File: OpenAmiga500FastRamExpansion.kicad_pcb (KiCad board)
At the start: 2 copper layers, 99.7 x 69.1 mm, 35 parts, among them J1 68000_SOCKET, P1 JTAG_CONNECTOR, P99 OSHW_LOGO, U1 68000D, U2 74LS157, U3 74LS157, U4 ATF1502AS-10JU44, U5 HYB5118160BSJ, U6 HYB5118160BSJ, U7 HYB5118160BSJ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

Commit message: Completed routing of data bus from CPU to RAM
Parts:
- moved C2 135.5 mm to (146.2, 68.8)
- moved C3 68.7 mm to (176.7, 68.8)
- moved C15 9.20 mm to (238.6, 58.8)
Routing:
- net /d11: track 53.2 -> 92.7 mm, vias 0 -> 1
- net /d12: track 53.1 -> 90.0 mm, vias 0 -> 1
- net /d13: track 53.2 -> 89.3 mm, vias 0 -> 1
- net /d14: track 53.2 -> 88.4 mm, vias 0 -> 1
- net /d15: track 53.1 -> 86.5 mm, vias 0 -> 1
- net VCC: track 7.11 -> 14.6 mm
- net /d10: track 96.0 -> 94.2 mm
- net /d8: track 98.5 -> 96.9 mm
- net /d9: track 97.3 -> 96.5 mm

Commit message: Almost there...
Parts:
- C13, C14, C15, C16, C17, C18, C19, C5, C6, C8: moved to B.Cu
- U4: footprint Package_LCC:PLCC-44_THT-Socket -> OpenAmiga500FastRamExpansion:PLCC-44_THT-Socket
- moved C19 185.7 mm to (111.2, 113.3), turned to 0 degrees
- moved C12 149.2 mm to (142.7, 94.2), turned to 0 degrees
- moved C8 141.0 mm to (159.3, 94.2), turned to 0 degrees
- moved C11 138.1 mm to (142.7, 87.9)
- moved C9 121.0 mm to (159.3, 87.9)
- moved C15 116.8 mm to (127.2, 93.7)
- moved C10 115.0 mm to (159.3, 113.3), turned to 0 degrees
- moved C18 110.3 mm to (111.2, 94.2)
- moved C5 107.0 mm to (180.7, 101.6), turned to 180 degrees
- moved C17 105.2 mm to (111.2, 87.9)
- moved C16 103.2 mm to (127.2, 113.3)
- moved C7 97.3 mm to (170.3, 98.8), turned to 90 degrees
- moved C13 94.7 mm to (142.7, 113.3), turned to 0 degrees
- moved C1 94.3 mm to (103.1, 117.2)
- moved C14 90.1 mm to (127.2, 87.9)
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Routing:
- net VCC: track 14.6 -> 523.3 mm, vias 0 -> 14
- net /a23: track 3.56 -> 117.0 mm
- net /a22: track 3.56 -> 110.4 mm
- net /a21: track 3.56 -> 104.4 mm
- net /~as: track 3.56 -> 98.9 mm
- net /a17: track 3.56 -> 91.3 mm, vias 0 -> 1
- net /a20: track 3.56 -> 91.1 mm
- net /~uds: track 3.56 -> 90.3 mm
- net /~ras3: track 0.00 -> 86.0 mm, vias 0 -> 1
- net /a19: track 3.56 -> 84.9 mm
- net /a18: track 17.2 -> 97.8 mm
- net /~ras2: track 0.00 -> 74.1 mm, vias 0 -> 1
- net /a16: track 11.8 -> 84.5 mm
- net /~ras1: track 0.00 -> 69.7 mm, vias 0 -> 1
- net /~lds: track 3.56 -> 71.0 mm
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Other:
- board size 99.7 x 69.1 mm -> 99.7 x 71.2 mm

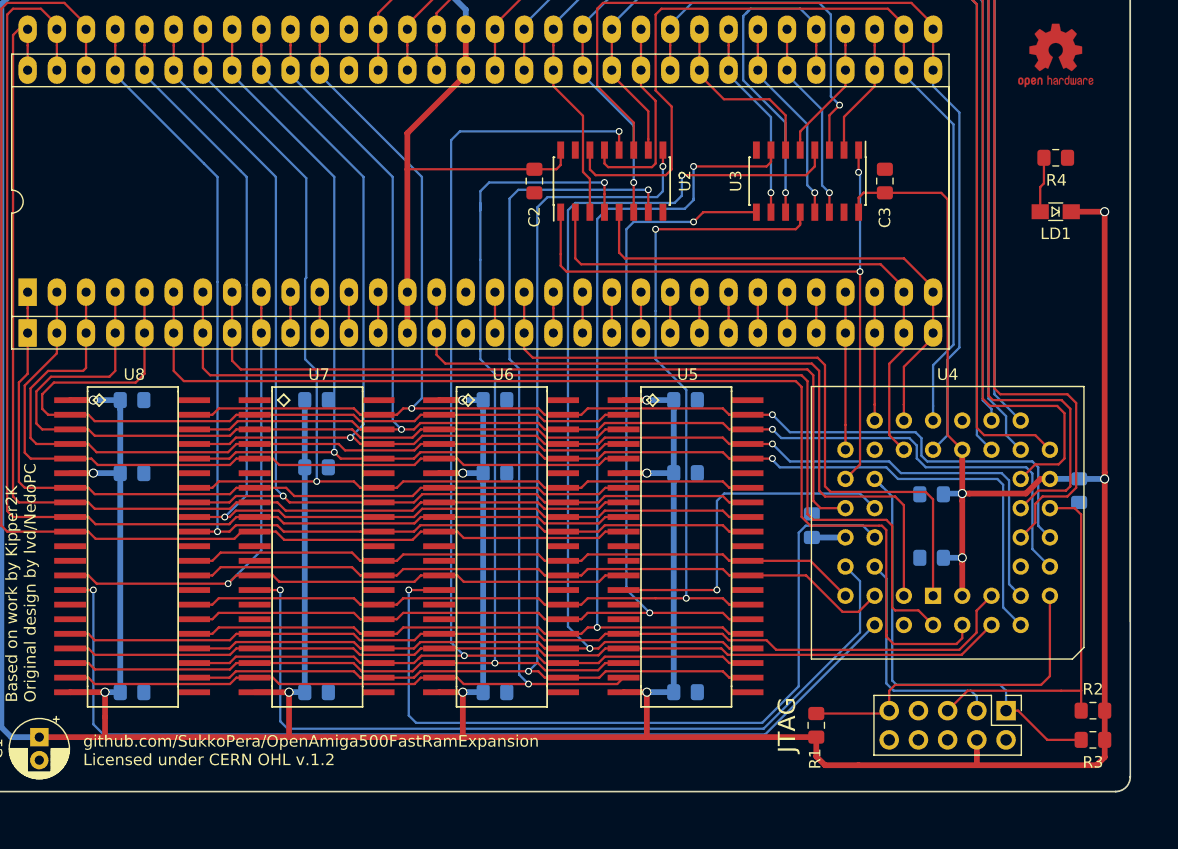
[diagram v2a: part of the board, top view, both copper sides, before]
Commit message: Routing complete Ground stitching and some refinements TBD
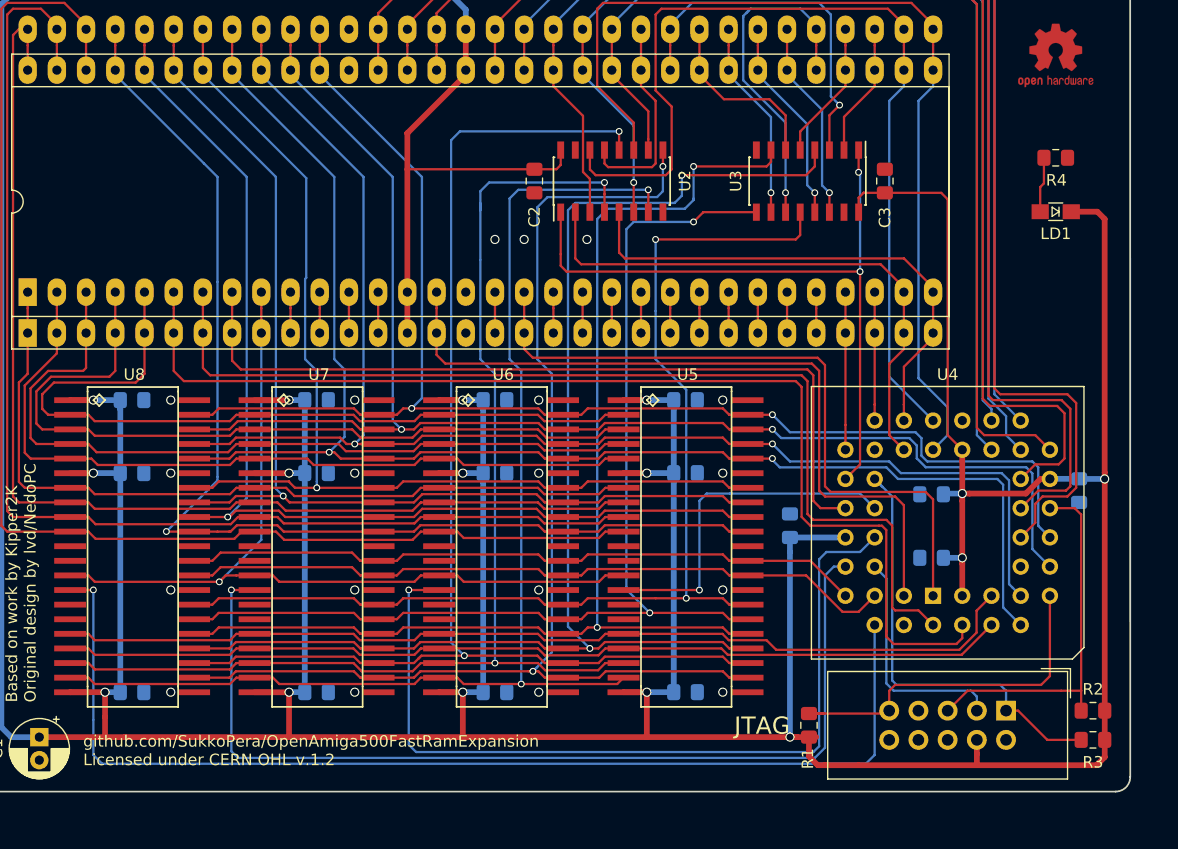
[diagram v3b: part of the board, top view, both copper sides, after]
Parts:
- P1: footprint Connector_PinHeader_2.54mm:PinHeader_2x05_P2.54mm_Vertical -> Connector_IDC:IDC-Header_2x05_P2.54mm_Vertical
- moved C8 6.35 mm to (159.3, 87.9)
- moved C9 6.35 mm to (159.3, 94.2)
- moved C7 1.91 mm to (168.4, 98.8)
- moved R1 0.63 mm to (170.1, 116.2)
- moved C15 0.51 mm to (127.2, 94.2)
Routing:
- net VCC: track 523.3 -> 551.6 mm, vias 14 -> 16
- net /~ras2: track 74.1 -> 85.4 mm
- net /~ras3: track 86.0 -> 96.3 mm
- net /~ras1: track 69.7 -> 74.1 mm
- net /d8: track 96.9 -> 101.1 mm
- net /d13: track 123.8 -> 125.8 mm
- net /ma4: track 105.3 -> 106.7 mm
- net /jtag_tdi: track 29.7 -> 30.9 mm
- net /d12: track 126.1 -> 127.0 mm
- net /d11: track 93.0 -> 93.6 mm
- net GND: vias 0 -> 19

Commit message: Refinements here and there
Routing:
- net /ma4: track 106.7 -> 106.1 mm

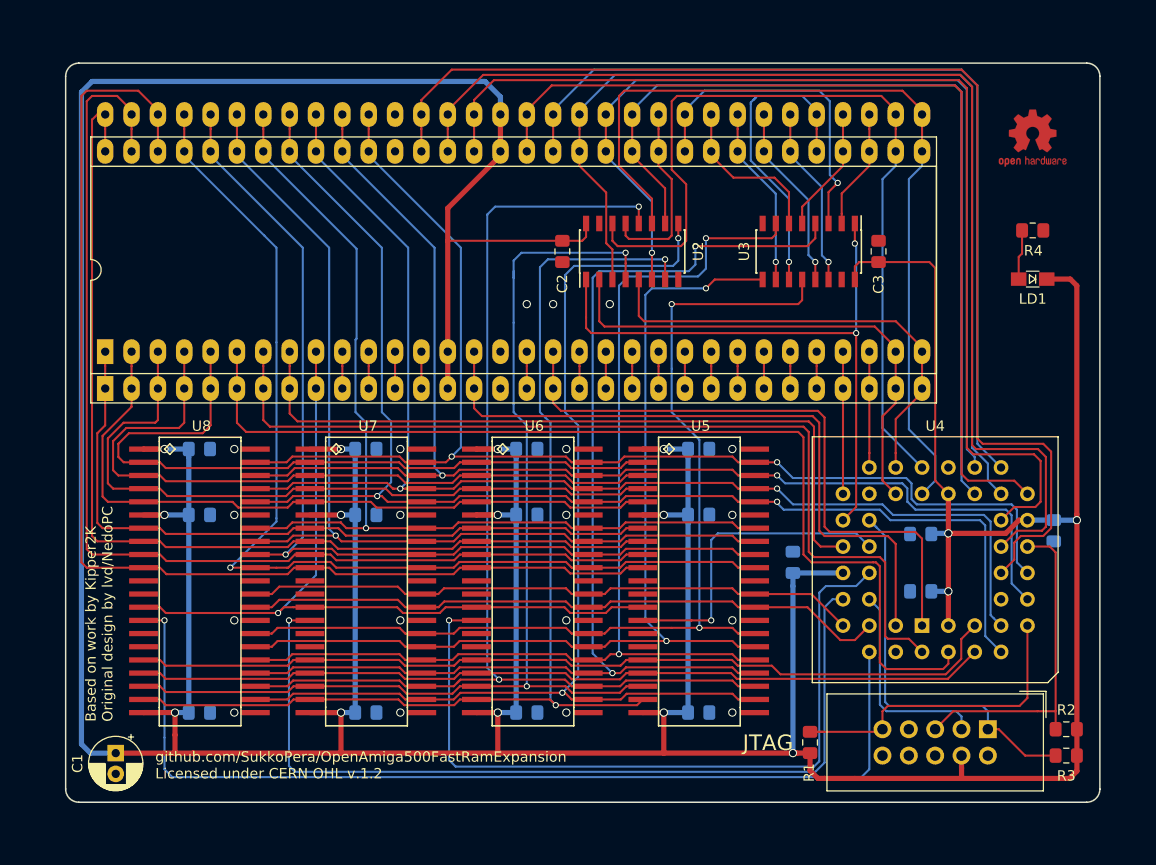
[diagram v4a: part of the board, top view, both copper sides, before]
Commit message: Stitched perimeter and more refinements
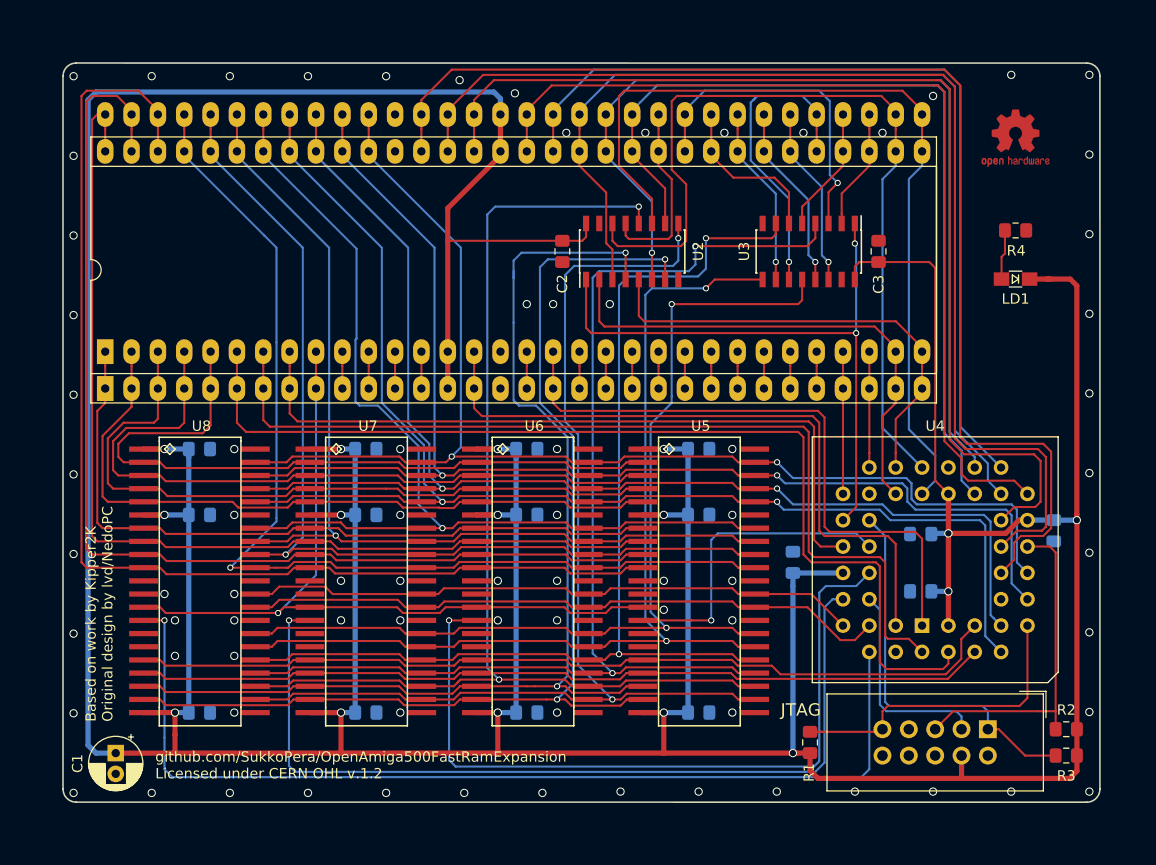
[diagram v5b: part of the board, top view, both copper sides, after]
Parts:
- moved LD1 1.65 mm to (189.9, 71.5)
- moved P99 1.65 mm to (189.9, 57.9)
- moved R4 1.65 mm to (189.9, 66.8)
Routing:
- net /d11: track 93.6 -> 97.7 mm
- net /ma2: track 105.6 -> 108.6 mm
- net /d12: track 127.0 -> 129.0 mm
- net /ma4: track 106.1 -> 107.5 mm
- net /d13: track 125.8 -> 126.9 mm
- net /a19: track 84.9 -> 83.9 mm
- net /a17: track 91.3 -> 90.3 mm
- net /a20: track 91.1 -> 90.1 mm
- net /a18: track 97.8 -> 96.8 mm
- net /a16: track 84.5 -> 83.5 mm
- net /ma3: track 106.7 -> 107.5 mm
- net VCC: track 551.3 -> 550.7 mm
- net /a21: track 104.4 -> 103.8 mm
- net GND: vias 19 -> 78
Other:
- board size 99.7 x 71.2 mm -> 100 x 71.3 mm

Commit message: More and more and more and more and more refinements...
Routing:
- net /d5: track 100.0 -> 96.0 mm
- net /~ras2: track 85.4 -> 84.8 mm
- net GND: vias 78 -> 84
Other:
- board size 100 x 71.3 mm -> 100 x 71.5 mm

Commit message: Add JTAG connector pinout
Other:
- board text added: "TCK"
- board text added: "TDI"
- board text added: "TDO"
- board text added: "TMS"
- board text removed: "1"
- board text removed: "1. TCK 2. GND 3. TDO 4. VCC"
- board text removed: "10"
- board text removed: "2"
- board text removed: "3"
- board text removed: "4"
- board text removed: "5"
- board text removed: "5. TMS 9. TDI 10. GND"
- board text removed: "6"
- board text removed: "7"
- board text removed: "8"
- board text removed: "9"
- board text removed: "JTAG PINOUT"
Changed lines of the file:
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@@
   (general
     (thickness 1.6)
-    (drawings 108)
+    (drawings 90)
     (tracks 1421)
     (zones 0)
@@
     )
   )
+  (gr_text GND (at 177.038 119.38) (layer B.SilkS)
+    (effects (font (size 0.7 0.7) (thickness 0.15)) (justify mirror))
+  )
+  (gr_text GND (at 187.198 119.38) (layer B.SilkS)
+    (effects (font (size 0.7 0.7) (thickness 0.15)) (justify mirror))
+  )
+  (gr_text VCC (at 184.658 119.38) (layer B.SilkS)
+    (effects (font (size 0.7 0.7) (thickness 0.15)) (justify mirror))
+  )
+  (gr_text TDI (at 177.038 113.03) (layer B.SilkS)
+    (effects (font (size 0.7 0.7) (thickness 0.15)) (justify mirror))
+  )
+  (gr_text TMS (at 182.118 113.03) (layer B.SilkS)
+    (effects (font (size 0.7 0.7) (thickness 0.15)) (justify mirror))
+  )
+  (gr_text TDO (at 184.658 113.03) (layer B.SilkS)
+    (effects (font (size 0.7 0.7) (thickness 0.15)) (justify mirror))
+  )
+  (gr_text TCK (at 187.198 113.03) (layer B.SilkS)
+    (effects (font (size 0.7 0.7) (thickness 0.15)) (justify mirror))
+  )
   (gr_arc (start 99.314 51.689) (end 99.314 50.419) (angle -90) (layer Edge.Cuts) (width 0.15))
   (gr_arc (start 99.314 120.65) (end 98.044 120.65) (angle -90) (layer Edge.Cuts) (width 0.15))
@@
   (gr_line (start 197.993 51.689) (end 197.995 120.658) (layer Edge.Cuts) (width 0.15))
   (gr_line (start 99.314 50.419) (end 196.725 50.427) (layer Edge.Cuts) (width 0.15))
-  (gr_arc (start 29.212 70.5565) (end 29.212 70.0485) (angle -90) (layer B.SilkS) (width 0.2))
-  (gr_arc (start 29.212 80.4625) (end 28.704 80.4625) (angle -90) (layer B.SilkS) (width 0.2))
-  (gr_arc (start 54.2945 80.4625) (end 54.2945 80.9705) (angle -90) (layer B.SilkS) (width 0.2))
-  (gr_arc (start 54.2945 70.5565) (end 54.8025 70.5565) (angle -90) (layer B.SilkS) (width 0.2))
-  (gr_line (start 29.212 70.0485) (end 54.2945 70.0485) (layer B.SilkS) (width 0.2))
-  (gr_line (start 28.704 80.4625) (end 28.704 70.5565) (layer B.SilkS) (width 0.2))
-  (gr_line (start 54.2945 80.9705) (end 29.212 80.9705) (layer B.SilkS) (width 0.2))
-  (gr_line (start 54.8025 70.5565) (end 54.8025 80.4625) (layer B.SilkS) (width 0.2))
-  (gr_text "5. TMS\n9. TDI\n10. GND" (at 35.6255 74.684) (layer B.SilkS)
-    (effects (font (size 1 1) (thickness 0.2)) (justify left mirror))
-  )
-  (gr_text "1. TCK\n2. GND\n3. TDO\n4. VCC" (at 41.785 75.534) (layer B.SilkS)
-    (effects (font (size 1 1) (thickness 0.2)) (justify left mirror))
-  )
-  (gr_text "JTAG\nPINOUT" (at 48.1985 73.0965) (layer B.SilkS)
-    (effects (font (size 1.5 1.5) (thickness 0.3)) (justify mirror))
-  )
-  (gr_line (start 43.055 76.133498) (end 43.055 80.070498) (layer B.SilkS) (width 0.2))
-  (gr_line (start 53.215 76.133498) (end 43.055 76.133498) (layer B.SilkS) (width 0.2))
-  (gr_line (start 53.215 80.070498) (end 53.215 76.133498) (layer B.SilkS) (width 0.2))
-  (gr_line (start 43.055 80.070498) (end 53.215 80.070498) (layer B.SilkS) (width 0.2))
-  (gr_text 9 (at 51.564 77.149498) (layer B.SilkS)
+  (gr_text V1 (at 195.834 119.888) (layer B.SilkS)
     (effects (font (size 1 1) (thickness 0.2)) (justify mirror))
   )
-  (gr_text 10 (at 51.564 78.927498) (layer B.SilkS)
-    (effects (font (size 1 1) (thickness 0.2)) (justify mirror))
-  )
-  (gr_text 7 (at 49.69075 77.149498) (layer B.SilkS)
-    (effects (font (size 1 1) (thickness 0.2)) (justify mirror))
-  )
-  (gr_text 5 (at 48.0715 77.149498) (layer B.SilkS)
-    (effects (font (size 1 1) (thickness 0.2)) (justify mirror))
-  )
-  (gr_text 8 (at 49.69075 78.927498) (layer B.SilkS)
-    (effects (font (size 1 1) (thickness 0.2)) (justify mirror))
-  )
-  (gr_text 6 (at 48.0715 78.927498) (layer B.SilkS)
-    (effects (font (size 1 1) (thickness 0.2)) (justify mirror))
-  )
-  (gr_text 3 (at 46.4205 77.149498) (layer B.SilkS)
-    (effects (font (size 1 1) (thickness 0.2)) (justify mirror))
-  )
-  (gr_text 4 (at 46.4205 78.927498) (layer B.SilkS)
-    (effects (font (size 1 1) (thickness 0.2)) (justify mirror))
-  )
-  (gr_text 1 (at 44.833 77.149498) (layer B.SilkS)
-    (effects (font (size 1 1) (thickness 0.2)) (justify mirror))
-  )
-  (gr_text 2 (at 44.833 78.927498) (layer B.SilkS)
-    (effects (font (size 1 1) (thickness 0.2)) (justify mirror))
-  )
-  (gr_text V1 (at 195.836 120.404) (layer B.SilkS)
-    (effects (font (size 1 1) (thickness 0.2)) (justify mirror))
-  )
